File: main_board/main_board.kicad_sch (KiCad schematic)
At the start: 56 parts, among them J1 USB4105-GF-A-060, J2 Conn_01x06_Pin, Q3 NX3008PBK,215, U1 SSD1306, U2 ESP32-S2-SOLO, U3 TLV62568PDRLT, U4 MCP73832, U5 DW01, U6 8205A, U7 MAX17055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

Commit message: Finalize frontend
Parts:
- M1: footprint main_board_parts:ECG-module -> main_board_parts:ECG-module_1lead
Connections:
- net +3V3: now also M1.14 (DVDD); no longer M1.12 (DVDD)
- net +BATT: now also M1.7 (VBAT); no longer M1.5 (VBAT)
- net ANALOG_EN: now also M1.16 (~{PDN}/~{RESET}); no longer M1.14 (~{PDN}/~{RESET})
- net ECG_CLK_EN: now also M1.15 (CLK_EN); no longer M1.13 (CLK_EN)
- net ECG_CS: now also M1.8 (~{CS}); no longer M1.6 (~{CS})
- net GND: now also M1.13 (DGND); no longer M1.11 (DGND)
- net GNDA: now also M1.6 (GNDA); no longer M1.4 (GNDA)
- net ~{TOUCH}: now also M1.17 (~{TOUCH}); no longer M1.15 (~{TOUCH})
- net at U2.4 (IO4): now also M1.12 (~{DRDY}); no longer M1.10 (~{DRDY})
- net at U2.5 (IO5): now also M1.11 (MISO); no longer M1.9 (MISO)
- net at U2.6 (IO6): now also M1.10 (SCLK); no longer M1.8 (SCLK)
- net at U2.7 (IO7): now also M1.9 (MOSI); no longer M1.7 (MOSI)
- no-connect marks 7 -> 9
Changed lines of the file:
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@@
   (title_block
     (title "Card/IO ECG main board")
-    (date "2023-09-11")
+    (date "2023-11-04")
     (rev "5")
   )
@@
   )
   (no_connect (at 254 109.22))
+  (no_connect (at 59.69 63.5))
   (no_connect (at 198.12 144.78))
   (no_connect (at 139.7 170.18))
   (no_connect (at 139.7 172.72))
+  (no_connect (at 57.15 63.5))
   (no_connect (at 198.12 147.32))
   (no_connect (at 81.28 162.56))
@@
     (stroke (width 0) (type default))
   )
-  (wire (pts (xy 60.96 33.02) (xy 60.96 34.29))
+  (wire (pts (xy 54.61 33.02) (xy 54.61 34.29))
     (stroke (width 0) (type default))
   )
@@
     (stroke (width 0) (type default))
   )
-  (wire (pts (xy 40.64 74.93) (xy 60.96 74.93))
+  (wire (pts (xy 40.64 74.93) (xy 54.61 74.93))
     (stroke (width 0) (type default))
   )
@@
     (stroke (width 0) (type default))
   )
-  (wire (pts (xy 72.39 30.48) (xy 58.42 30.48))
+  (wire (pts (xy 66.04 30.48) (xy 52.07 30.48))
     (stroke (width 0) (type default))
   )
@@
     (stroke (width 0) (type default))
   )
-  (wire (pts (xy 60.96 33.02) (xy 72.39 33.02))
+  (wire (pts (xy 54.61 33.02) (xy 66.04 33.02))
     (stroke (width 0) (type default))
   )
@@
     (stroke (width 0) (type default))
   )
-  (wire (pts (xy 58.42 63.5) (xy 58.42 76.2))
+  (wire (pts (xy 52.07 63.5) (xy 52.07 76.2))
     (stroke (width 0) (type default))
   )
@@
     (stroke (width 0) (type default))
   )
-  (wire (pts (xy 58.42 30.48) (xy 58.42 34.29))
+  (wire (pts (xy 52.07 30.48) (xy 52.07 34.29))
     (stroke (width 0) (type default))
   )
@@
     (stroke (width 0) (type default))
   )
-  (wire (pts (xy 60.96 63.5) (xy 60.96 74.93))
+  (wire (pts (xy 54.61 63.5) (xy 54.61 74.93))
     (stroke (width 0) (type default))
   )
@@
     (stroke (width 0) (type default))
   )
-  (wire (pts (xy 55.88 63.5) (xy 55.88 66.04))
-    (stroke (width 0) (type default))
-  )
   (wire (pts (xy 254 143.51) (xy 254 147.32))
     (stroke (width 0) (type default))
   )
-  (wire (pts (xy 40.64 66.04) (xy 55.88 66.04))
+  (wire (pts (xy 40.64 66.04) (xy 49.53 66.04))
     (stroke (width 0) (type default))
   )
@@
     (stroke (width 0) (type default))
   )
-  (wire (pts (xy 40.64 76.2) (xy 58.42 76.2))
+  (wire (pts (xy 40.64 76.2) (xy 52.07 76.2))
     (stroke (width 0) (type default))
   )
@@
     (stroke (width 0) (type default))
   )
+  (wire (pts (xy 49.53 63.5) (xy 49.53 66.04))
+    (stroke (width 0) (type default))
+  )
   (wire (pts (xy 201.93 111.76) (xy 208.28 111.76))
     (stroke (width 0) (type default))
@@
     (stroke (width 0) (type default))
   )
-  (wire (pts (xy 55.88 27.94) (xy 72.39 27.94))
+  (wire (pts (xy 49.53 27.94) (xy 66.04 27.94))
     (stroke (width 0) (type default))
   )
@@
     (stroke (width 0) (type default))
   )
-  (wire (pts (xy 55.88 34.29) (xy 55.88 27.94))
+  (wire (pts (xy 49.53 34.29) (xy 49.53 27.94))
     (stroke (width 0) (type default))
   )
@@
     (effects (font (size 1.27 1.27)) (justify left bottom))
   )
-  (label "ANALOG_EN" (at 72.39 30.48 180) (fields_autoplaced)
+  (label "ANALOG_EN" (at 66.04 30.48 180) (fields_autoplaced)
     (effects (font (size 1.27 1.27)) (justify right bottom))
   )
@@
     (effects (font (size 1.27 1.27)) (justify right bottom))
   )
-  (label "~{TOUCH}" (at 72.39 27.94 180) (fields_autoplaced)
+  (label "~{TOUCH}" (at 66.04 27.94 180) (fields_autoplaced)
     (effects (font (size 1.27 1.27)) (justify right bottom))
   )
@@
     (effects (font (size 1.27 1.27)) (justify left bottom))
   )
-  (label "ECG_CLK_EN" (at 72.39 33.02 180) (fields_autoplaced)
+  (label "ECG_CLK_EN" (at 66.04 33.02 180) (fields_autoplaced)
     (effects (font (size 1.27 1.27)) (justify right bottom))
   )
@@
       (effects (font (size 1.27 1.27)))
     )
-    (property "Footprint" "main_board_parts:ECG-module" (at 71.12 48.26 0)
+    (property "Footprint" "main_board_parts:ECG-module_1lead" (at 71.12 48.26 0)
       (effects (font (size 1.27 1.27)) hide)
     )
@@
     (pin "14")
     (pin "15")
+    (pin "16")
+    (pin "17")
     (pin "2")
     (pin "3")

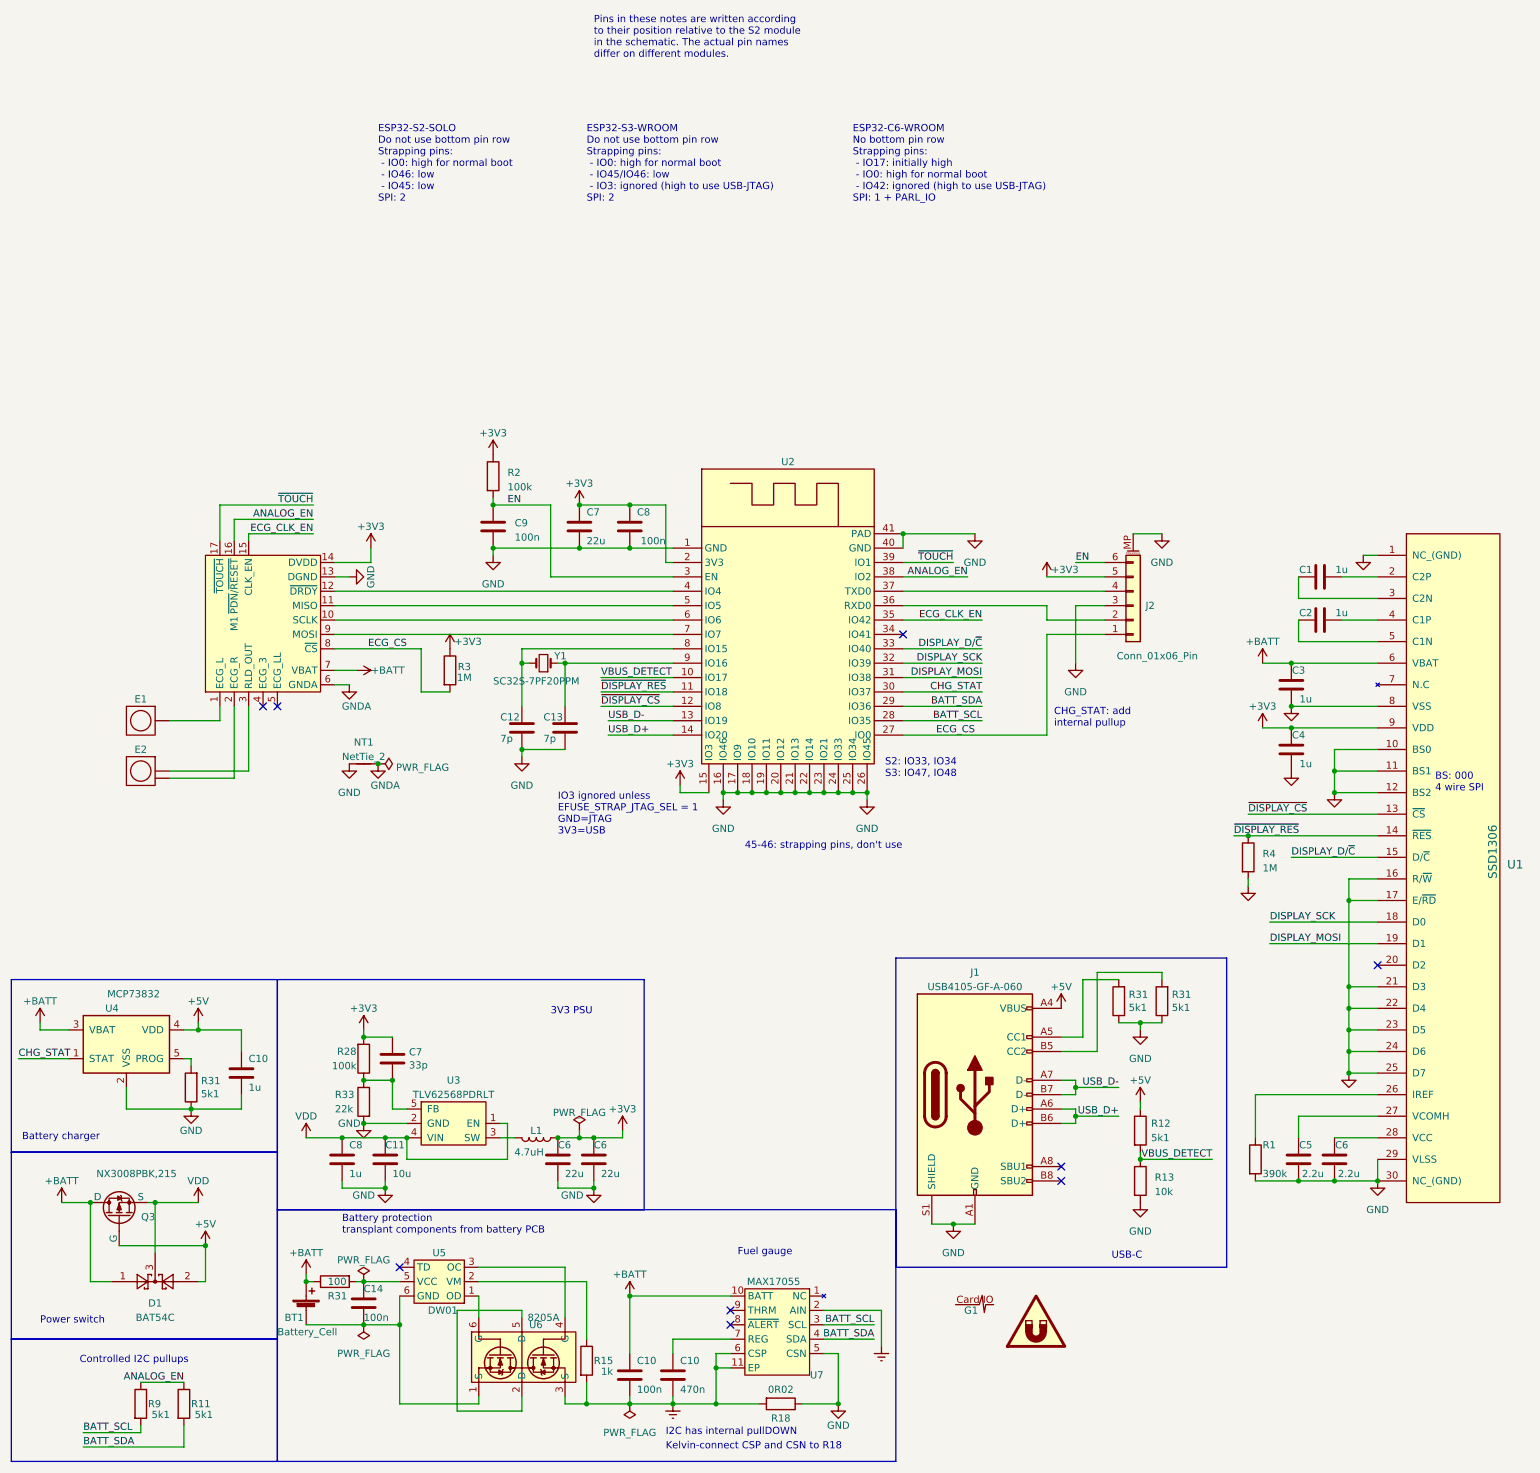
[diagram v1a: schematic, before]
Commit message: Separate frontend reset from system enable
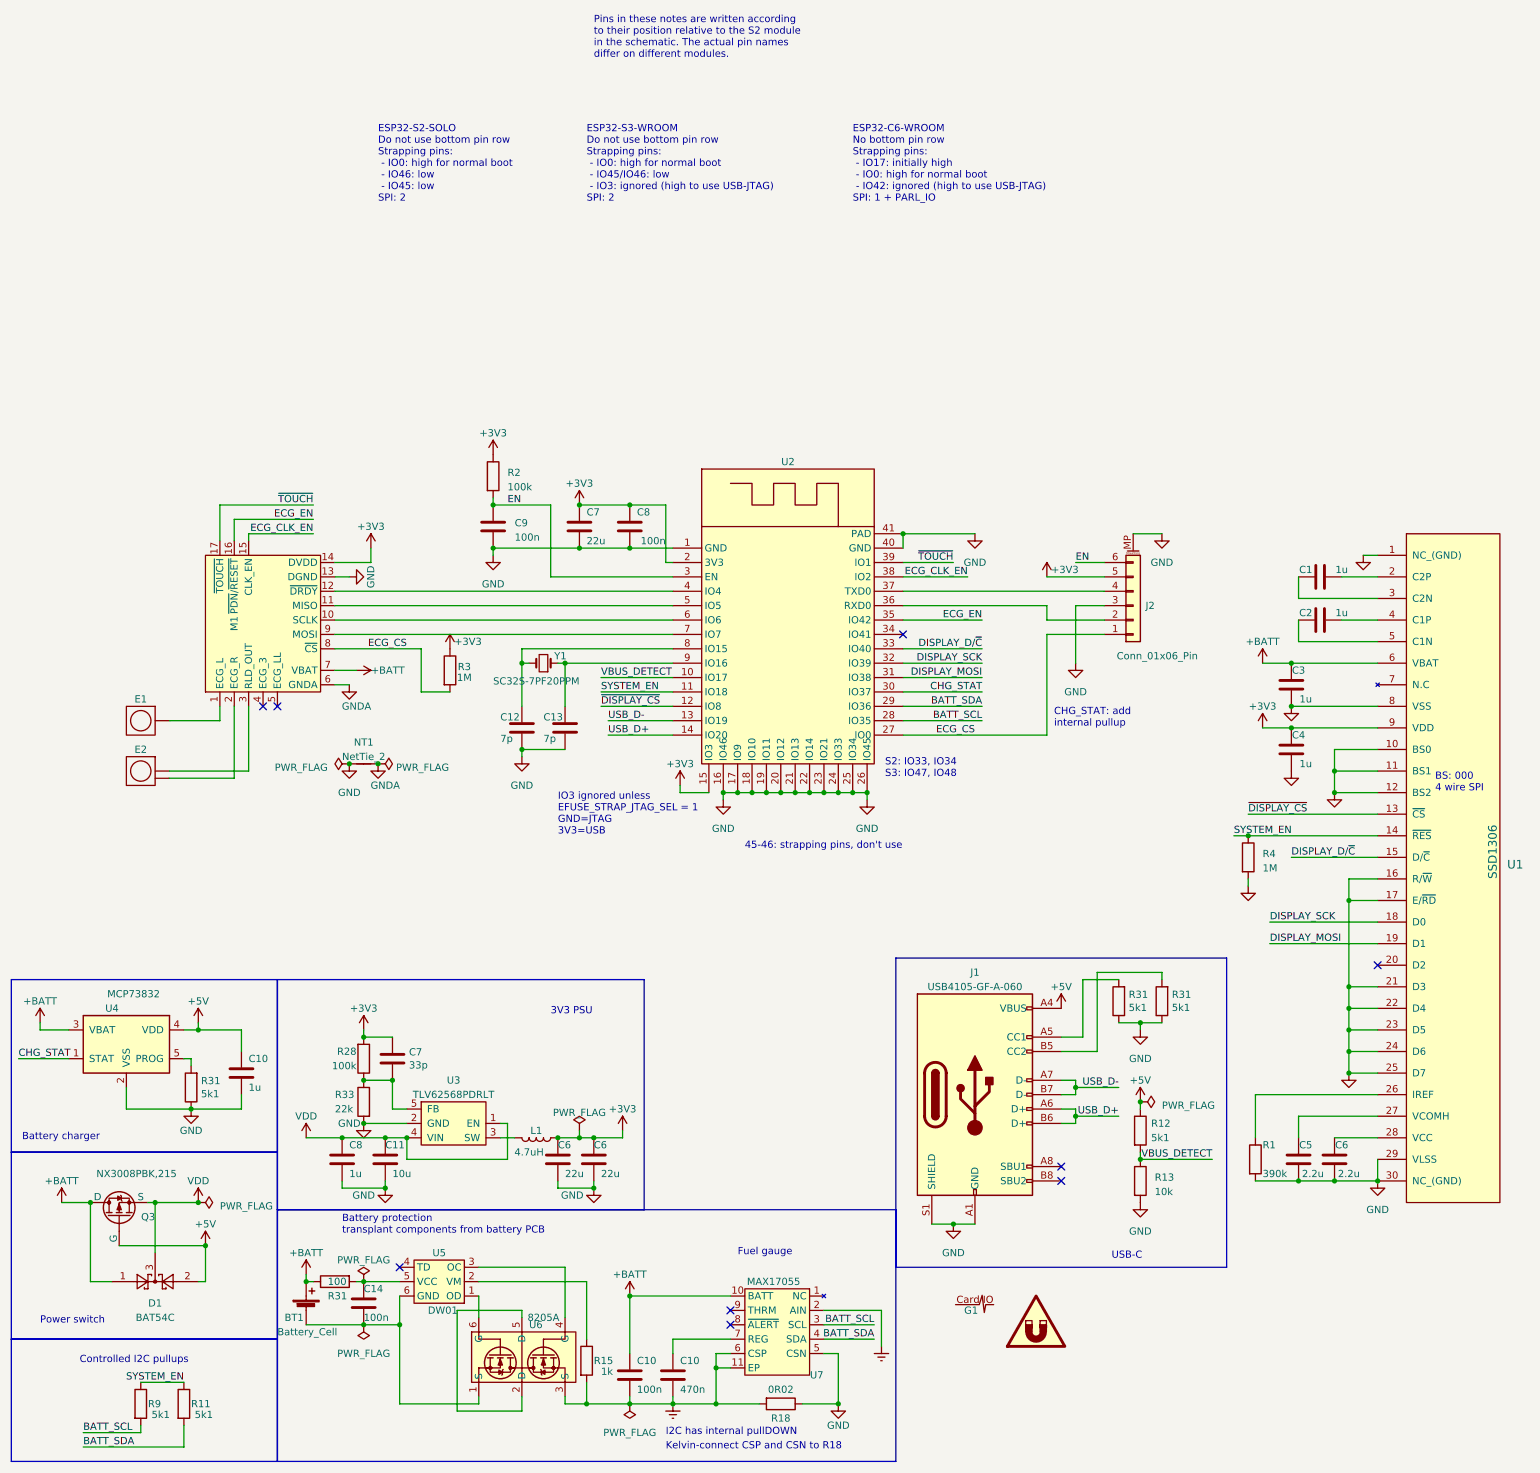
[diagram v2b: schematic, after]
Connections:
- net ~{DISPLAY_RES} is gone; now on net SYSTEM_EN: R4.1, U1.14 (~{RES}), U2.11 (IO18)
- net ECG_CLK_EN: now also U2.38 (IO2); no longer U2.35 (IO42)
- net ANALOG_EN renamed SYSTEM_EN
- net SYSTEM_EN: no longer M1.16 (~{PDN}/~{RESET}), U2.38 (IO2)
- new net ECG_EN: M1.16 (~{PDN}/~{RESET}), U2.35 (IO42)
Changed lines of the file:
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@@
   (title_block
     (title "Card/IO ECG main board")
-    (date "2023-11-04")
-    (rev "5")
+    (date "2023-11-05")
+    (rev "6")
   )
   (junction (at 200.66 135.89) (diameter 0) (color 0 0 0 0)
@@
   (junction (at 26.67 151.13) (diameter 0) (color 0 0 0 0)
   )
+  (junction (at 212.09 133.35) (diameter 0) (color 0 0 0 0)
+  )
   (junction (at 113.03 35.56) (diameter 0) (color 0 0 0 0)
   )
@@
   (junction (at 231.14 86.36) (diameter 0) (color 0 0 0 0)
   )
+  (junction (at 45.72 151.13) (diameter 0) (color 0 0 0 0)
+  )
   (junction (at 45.72 120.65) (diameter 0) (color 0 0 0 0)
   )
@@
   (junction (at 248.92 120.65) (diameter 0) (color 0 0 0 0)
   )
+  (junction (at 72.39 73.66) (diameter 0) (color 0 0 0 0)
+  )
   (junction (at 179.07 154.94) (diameter 0) (color 0 0 0 0)
   )
@@
     (stroke (width 0) (type default))
   )
+  (wire (pts (xy 121.92 167.64) (xy 139.7 167.64))
+    (stroke (width 0) (type default))
+  )
   (wire (pts (xy 240.03 147.32) (xy 246.38 147.32))
     (stroke (width 0) (type default))
@@
     (stroke (width 0) (type default))
   )
-  (wire (pts (xy 121.92 167.64) (xy 139.7 167.64))
-    (stroke (width 0) (type default))
-  )
   (wire (pts (xy 251.46 36.83) (xy 254 36.83))
     (stroke (width 0) (type default))
@@
     (effects (font (size 1.27 1.27)) (justify right bottom))
   )
-  (label "~{DISPLAY_RES}" (at 228.6 86.36 0) (fields_autoplaced)
-    (effects (font (size 1.27 1.27)) (justify left bottom))
-  )
   (label "EN" (at 100.33 27.94 0) (fields_autoplaced)
     (effects (font (size 1.27 1.27)) (justify left bottom))
   )
-  (label "ANALOG_EN" (at 181.61 40.64 180) (fields_autoplaced)
-    (effects (font (size 1.27 1.27)) (justify right bottom))
+  (label "SYSTEM_EN" (at 116.84 60.96 0) (fields_autoplaced)
+    (effects (font (size 1.27 1.27)) (justify left bottom))
   )
   (label "DISPLAY_D{slash}~{C}" (at 238.76 90.17 0) (fields_autoplaced)
     (effects (font (size 1.27 1.27)) (justify left bottom))
   )
-  (label "ANALOG_EN" (at 66.04 30.48 180) (fields_autoplaced)
+  (label "ECG_CS" (at 182.88 68.58 180) (fields_autoplaced)
     (effects (font (size 1.27 1.27)) (justify right bottom))
   )
-  (label "ECG_CS" (at 182.88 68.58 180) (fields_autoplaced)
+  (label "ECG_EN" (at 66.04 30.48 180) (fields_autoplaced)
     (effects (font (size 1.27 1.27)) (justify right bottom))
   )
@@
     (effects (font (size 1.27 1.27)) (justify right bottom))
   )
+  (label "ECG_CLK_EN" (at 66.04 33.02 180) (fields_autoplaced)
+    (effects (font (size 1.27 1.27)) (justify right bottom))
+  )
   (label "EN" (at 200.66 38.1 0) (fields_autoplaced)
     (effects (font (size 1.27 1.27)) (justify left bottom))
@@
     (effects (font (size 1.27 1.27)) (justify left bottom))
   )
-  (label "ECG_CLK_EN" (at 66.04 33.02 180) (fields_autoplaced)
-    (effects (font (size 1.27 1.27)) (justify right bottom))
+  (label "SYSTEM_EN" (at 228.6 86.36 0) (fields_autoplaced)
+    (effects (font (size 1.27 1.27)) (justify left bottom))
   )
   (label "DISPLAY_D{slash}~{C}" (at 184.15 53.34 180) (fields_autoplaced)
@@
     (effects (font (size 1.27 1.27)) (justify right bottom))
   )
-  (label "ANALOG_EN" (at 43.18 182.88 180) (fields_autoplaced)
+  (label "SYSTEM_EN" (at 43.18 182.88 180) (fields_autoplaced)
     (effects (font (size 1.27 1.27)) (justify right bottom))
   )
@@
     (effects (font (size 1.27 1.27)) (justify left bottom))
   )
-  (label "ECG_CLK_EN" (at 184.15 48.26 180) (fields_autoplaced)
+  (label "ECG_EN" (at 184.15 48.26 180) (fields_autoplaced)
     (effects (font (size 1.27 1.27)) (justify right bottom))
   )
-  (label "~{DISPLAY_RES}" (at 116.84 60.96 0) (fields_autoplaced)
-    (effects (font (size 1.27 1.27)) (justify left bottom))
+  (label "ECG_CLK_EN" (at 181.61 40.64 180) (fields_autoplaced)
+    (effects (font (size 1.27 1.27)) (justify right bottom))
   )
   (label "VBUS_DETECT" (at 224.79 143.51 180) (fields_autoplaced)
@@
     )
   )
+  (symbol (lib_id "power:PWR_FLAG") (at 45.72 151.13 270) (unit 1)
+    (in_bom yes) (on_board yes) (dnp no) (fields_autoplaced)
+    (property "Reference" "#FLG08" (at 47.625 151.13 0)
+      (effects (font (size 1.27 1.27)) hide)
+    )
+    (property "Value" "PWR_FLAG" (at 49.53 151.765 90)
+      (effects (font (size 1.27 1.27)) (justify left))
+    )
+    (property "Footprint" "" (at 45.72 151.13 0)
+      (effects (font (size 1.27 1.27)) hide)
+    )
+    (property "Datasheet" "~" (at 45.72 151.13 0)
+      (effects (font (size 1.27 1.27)) hide)
+    )
+    (pin "1")
+    (instances
+      (project "main_board"
+        (path "/e55848cd-275a-4b5e-8e68-b5d8d07c8d31"
+          (reference "#FLG08") (unit 1)
+        )
+      )
+    )
+  )
   (symbol (lib_id "power:+3V3") (at 76.2 35.56 0) (unit 1)
     (in_bom yes) (on_board yes) (dnp no) (fields_autoplaced)
@@
     )
   )
+  (symbol (lib_id "power:PWR_FLAG") (at 72.39 73.66 90) (unit 1)
+    (in_bom yes) (on_board yes) (dnp no) (fields_autoplaced)
+    (property "Reference" "#FLG06" (at 70.485 73.66 0)
+      (effects (font (size 1.27 1.27)) hide)
+    )
+    (property "Value" "PWR_FLAG" (at 68.58 74.295 90)
+      (effects (font (size 1.27 1.27)) (justify left))
+    )
+    (property "Footprint" "" (at 72.39 73.66 0)
+      (effects (font (size 1.27 1.27)) hide)
+    )
+    (property "Datasheet" "~" (at 72.39 73.66 0)
+      (effects (font (size 1.27 1.27)) hide)
+    )
+    (pin "1")
+    (instances
+      (project "main_board"
+        (path "/e55848cd-275a-4b5e-8e68-b5d8d07c8d31"
+          (reference "#FLG06") (unit 1)
+        )
+      )
+    )
+  )
   (symbol (lib_id "Connector_Generic_MountingPin:Conn_01x06_MountingPin") (at 210.82 45.72 0) (mirror x) (unit 1)
     (in_bom yes) (on_board yes) (dnp no)
@@
         )
       )
+    )
+  )
+  (symbol (lib_id "power:PWR_FLAG") (at 212.09 133.35 270) (unit 1)
+    (in_bom yes) (on_board yes) (dnp no) (fields_autoplaced)
+    (property "Reference" "#FLG07" (at 213.995 133.35 0)
+      (effects (font (size 1.27 1.27)) hide)
+    )
+    (property "Value" "PWR_FLAG" (at 215.9 133.985 90)
+      (effects (font (size 1.27 1.27)) (justify left))
+    )
+    (property "Footprint" "" (at 212.09 133.35 0)
+      (effects (font (size 1.27 1.27)) hide)
+    )
+    (property "Datasheet" "~" (at 212.09 133.35 0)
+      (effects (font (size 1.27 1.27)) hide)
+    )
+    (pin "1")
+    (instances
+      (project "main_board"
+        (path "/e55848cd-275a-4b5e-8e68-b5d8d07c8d31"
+          (reference "#FLG07") (unit 1)
+        )
+      )
